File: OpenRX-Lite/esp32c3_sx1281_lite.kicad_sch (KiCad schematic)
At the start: 40 parts, among them U1 ESP32-C3FH4, U2 TLV75533PDQNR, U3 SX1281IMLTRT, U4 RFX2401C, X1 CJ17-400001010B20

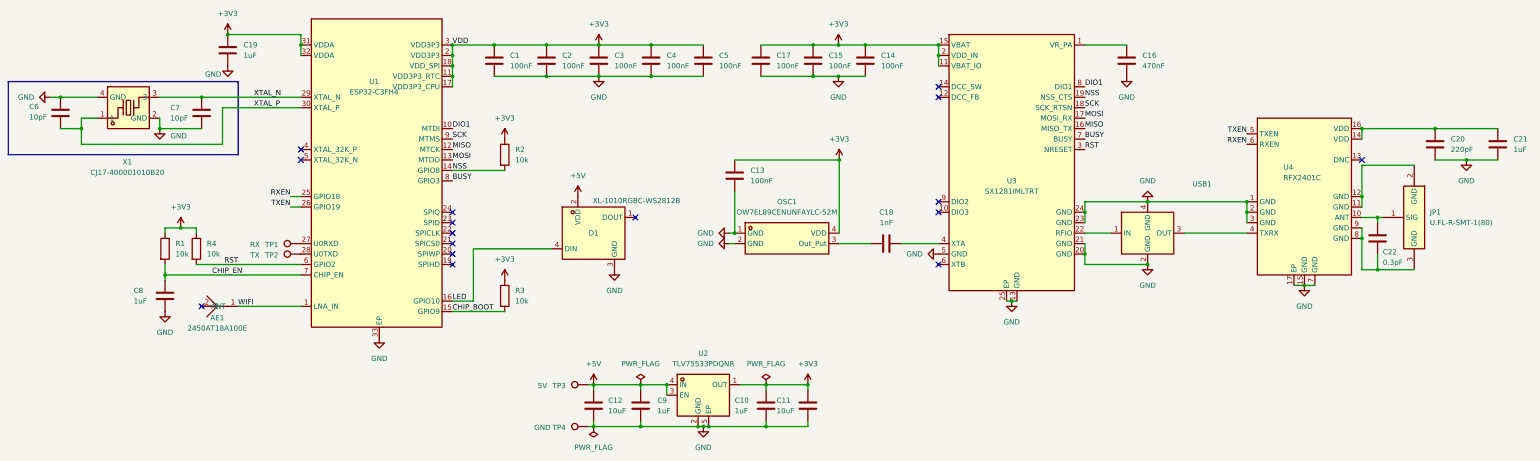
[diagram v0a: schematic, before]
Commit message: Separate Lite and Nano schematics, stop sharing one file
Sharing one .kicad_sch between projects doesn't work - KiCad
overwrites instance data when either project saves.

- Lite: restored pre-Nano schematic as local esp32c3_sx1281_lite.kicad_sch
- Nano: copied current shared sheet as local esp32c3_sx1281_rx_core.kicad_sch
- Each project now has its own schematic file
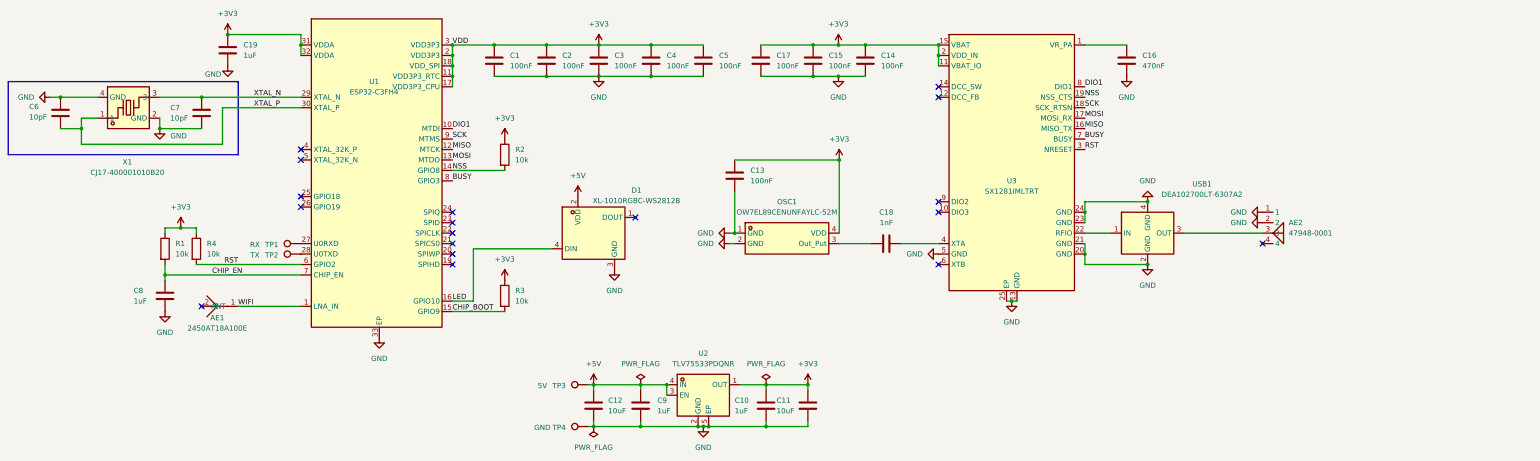
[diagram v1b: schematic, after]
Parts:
- removed C20: 220pF, Capacitor_SMD:C_0201_0603Metric, symbol Device:C
- removed C21: 1uF, Capacitor_SMD:C_0201_0603Metric, symbol Device:C
- removed C22: 0.3pF, Capacitor_SMD:C_0201_0603Metric, symbol Device:C
- removed JP1: U.FL-R-SMT-1(80), OpenRX-Shared:RF-SMD_FRF05002-JSS103M, symbol OpenRX-Shared:U.FL-R-SMT-1(80)
- removed U4: RFX2401C, OpenRX-Shared:QFN-16_L3.0-W3.0-P0.50-BL-EP1.7, symbol OpenRX-Shared:RFX2401C
- added AE2: 47948-0001, OpenRX-Shared:ANT-SMD_47948-0001, symbol OpenRX-Shared:47948-0001
- C1, C13, C14, C15, C17, C2, C3, C4, C5: LCSC C14858 -> (none)
- C10, C19, C8, C9: LCSC C77857 -> (none)
- C11, C12: LCSC C15525 -> (none)
- C16: LCSC C304534 -> (none)
- C18: LCSC C80390 -> (none)
- C6, C7: LCSC C14854 -> (none)
- R1, R2, R3, R4: LCSC C172043 -> (none)
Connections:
- net GND: now also AE2.1, AE2.2
- net at USB1.3 (OUT): now also AE2.3
- net RXEN: no longer names the net of U1.25 (GPIO18)
- net TXEN: no longer names the net of U1.26 (GPIO19)
- no-connect marks 16 -> 18

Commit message: Lite + Nano schematics: LCSC fields, fix 10uF to 0402, drop 0.3pF cap
- All passives in both schematics have LCSC fields
- 10uF caps fixed from 0201 to 0402 (C15525)
- Nano C22 (0.3pF): removed discrete cap, use trace capacitance instead
- 0 ERC errors on both schematics
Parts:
- AE1: LCSC (none) -> C89334
- AE2: LCSC (none) -> C152351
- C1, C13, C14, C15, C17, C2, C3, C4, C5: LCSC (none) -> C14858
- C10, C19, C8, C9: LCSC (none) -> C77857
- C11, C12: footprint Capacitor_SMD:C_0201_0603Metric -> Capacitor_SMD:C_0402_1005Metric; LCSC (none) -> C15525
- C16: LCSC (none) -> C304534
- C18: LCSC (none) -> C80390
- C6, C7: LCSC (none) -> C14854
- D1: LCSC (none) -> C5349953
- OSC1: LCSC (none) -> C22434896
- R1, R2, R3, R4: LCSC (none) -> C172043
- U1: LCSC (none) -> C2858491
- U2: LCSC (none) -> C2861882
- U3: LCSC (none) -> C2151551
- USB1: LCSC (none) -> C574024
- X1: LCSC (none) -> C2875272

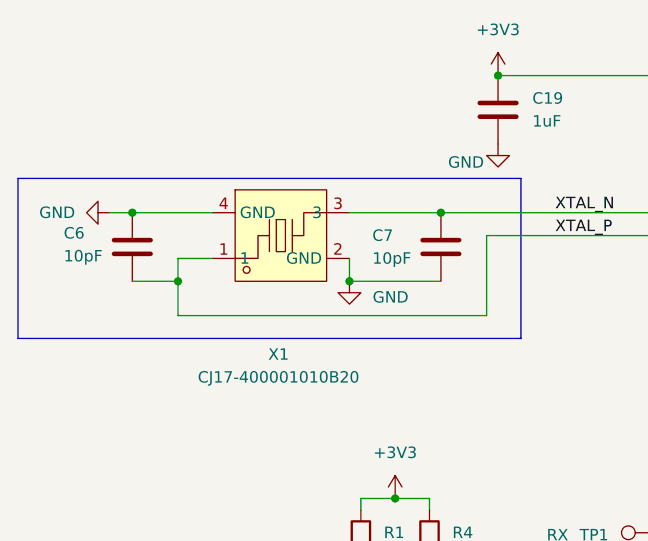
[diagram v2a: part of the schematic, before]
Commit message: Fix crystal load caps: 10pF → 18pF (C71153) on all 4 receivers
CJ17-400001010B20 crystal has CL=10pF. With 10pF load caps and
~2pF stray, effective load was only 7pF (30% low). Changed to 18pF
giving ~11pF effective load, matching the crystal spec.

C71153 = Samsung CL03C180JA3NNNC, 18pF C0G 25V 0201.
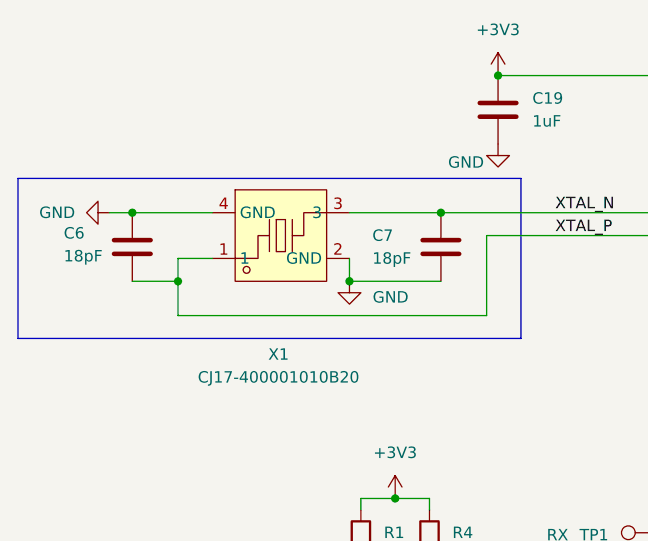
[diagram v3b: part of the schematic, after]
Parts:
- C6, C7: value 10pF -> 18pF; LCSC C14854 -> C71153
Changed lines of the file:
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@@
 			)
 		)
-		(property "Value" "10pF"
+		(property "Value" "18pF"
 			(at 66.04 46.99 0)
 			(show_name no)
@@
 			)
 		)
-		(property "LCSC" "C14854"
+		(property "LCSC" "C71153"
 			(at 0 0 0)
 			(show_name no)
@@
 			)
 		)
-		(property "Value" "10pF"
+		(property "Value" "18pF"
 			(at 31.75 46.736 0)
 			(show_name no)
@@
 			)
 		)
-		(property "LCSC" "C14854"
+		(property "LCSC" "C71153"
 			(at 0 0 0)
 			(show_name no)

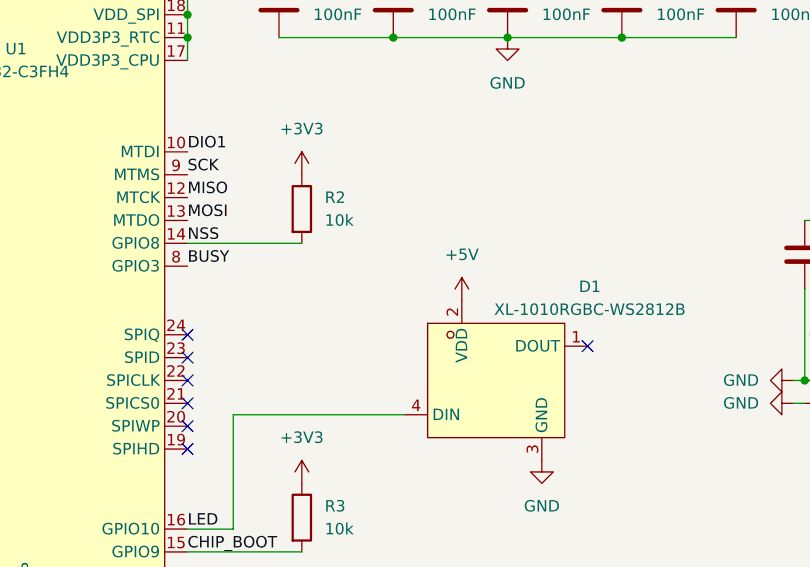
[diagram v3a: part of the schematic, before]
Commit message: Fix Gemini crystal load caps to 18pF (C62164), matching Lite and Mono
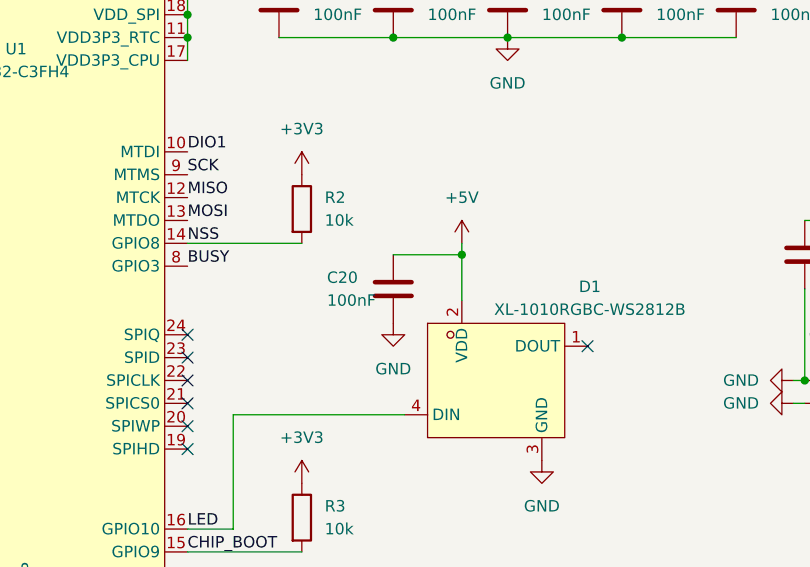
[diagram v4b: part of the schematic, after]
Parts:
- added C20: 100nF, Capacitor_SMD:C_0201_0603Metric, symbol Device:C
- C1, C13, C14, C15, C17, C2, C3, C4, C5: LCSC C14858 -> C76939
- C10, C19, C8, C9: LCSC C77857 -> C76935
- C16: LCSC C304534 -> C85926
- C18: LCSC C80390 -> C66942
- C6, C7: LCSC C71153 -> C62164
- R1, R2, R3, R4: LCSC C172043 -> C106225
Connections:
- net +5V: now also C20.1
- net GND: now also C20.2

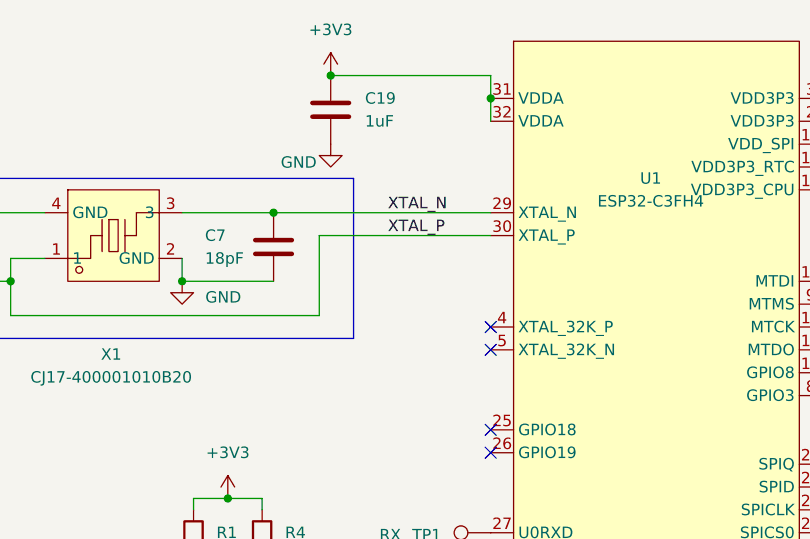
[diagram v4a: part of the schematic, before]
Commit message: OpenRX-Gemini: dual LR1121 schematic complete, 0 ERC errors
- Radio 1 (U4): sub-GHz via Johanson IPD → JP1 UFL
- Radio 2 (U9): 2.4GHz via RFX2401C (U10) → DEA (USB2) → JP3 UFL
- Shared SPI bus (SCK/MISO/MOSI), separate NSS/IRQ/BUSY/RST per radio
- Radio 2 control: GPIO10=NSS2, GPIO9=IRQ2, GPIO1=BUSY2, GPIO0=RST2
- FEM driven by Radio 2 RFSW (DIO5→RXEN, DIO6→TXEN)
- Radio 1 DIO5/DIO6 have 100k pull-downs (disconnected from FEM)
- No LED (GPIO10 used for NSS2), no boot button (GPIO9 used for IRQ2)
- Still needs: 10k pull-up on NSS2
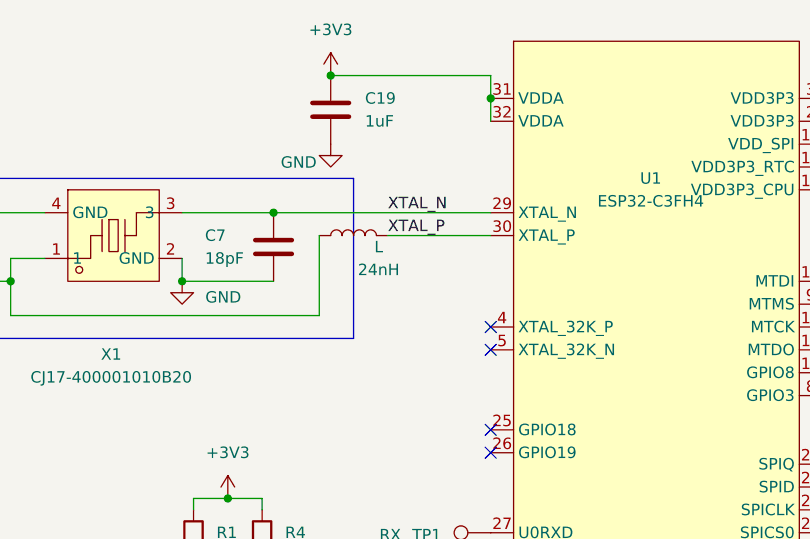
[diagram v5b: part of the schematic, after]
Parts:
- added L: 24nH, Inductor_SMD:L_0201_0603Metric, symbol Device:L
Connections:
- net XTAL_P: now also L.2; no longer C6.1, X1.1
- new net: C6.1, L.1, X1.1
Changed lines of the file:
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@@
+	(wire
+		(pts
+			(xy 86.36 44.45) (xy 97.79 44.45)
+		)
+		(stroke
+			(width 0)
+			(type default)
+		)
+	)
 	(wire
 		(pts
@@
 		(pts
 			(xy 64.77 85.09) (xy 64.77 82.55)
-		)
-		(stroke
-			(width 0)
-			(type default)
-		)
-	)
-	(wire
-		(pts
-			(xy 78.74 44.45) (xy 97.79 44.45)
 		)
 		(stroke
@@
 					(unit 1)
 				)
+			)
+		)
+	)
+	(symbol
+		(lib_id "Device:L")
+		(at 82.55 44.45 90)
+		(unit 1)
+		(body_style 1)
+		(exclude_from_sim no)
+		(in_bom yes)
+		(on_board yes)
+		(in_pos_files yes)
+		(dnp no)
+		(property "Reference" "L"
+			(at 85.344 45.72 90)
+			(show_name no)
+			(do_not_autoplace no)
+			(effects
+				(font
+					(size 1.27 1.27)
+				)
+			)
+		)
+		(property "Value" "24nH"
+			(at 85.344 48.26 90)
+			(show_name no)
+			(do_not_autoplace no)
+			(effects
+				(font
+					(size 1.27 1.27)
+				)
+			)
+		)
+		(property "Footprint" "Inductor_SMD:L_0201_0603Metric"
+			(at 82.55 44.45 0)
+			(hide yes)
+			(show_name no)
+			(do_not_autoplace no)
+			(effects
+				(font
+					(size 1.27 1.27)
+				)
+			)
+		)
+		(property "Datasheet" ""
+			(at 82.55 44.45 0)
+			(hide yes)
+			(show_name no)
+			(do_not_autoplace no)
+			(effects
+				(font
+					(size 1.27 1.27)
+				)
+			)
+		)
+		(property "Description" "Inductor"
+			(at 82.55 44.45 0)
+			(hide yes)
+			(show_name no)
+			(do_not_autoplace no)
+			(effects
+				(font
+					(size 1.27 1.27)
+				)
+			)
+		)
+		(property "LCSC" "C206441"
+			(at 82.55 44.45 0)
+			(hide yes)
+			(show_name no)
+			(do_not_autoplace no)
+			(effects
+				(font
+					(size 1.27 1.27)
+				)
+			)
+		)
+		(pin "2"
+		)
+		(pin "1"
+		)
+		(instances
+			(project "OpenRX-Lite"
+				(path "/8521861a-4fab-458b-8289-5e2efb91d906/d4225140-81df-42e7-abd7-e679e5ab5187"
+					(reference "L")
+					(unit 1)
+				)

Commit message: Swap all solder pads to 1.2x2.0mm rounded (25%) across Lite, Mono, Gemini
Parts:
- TP1, TP2, TP3, TP4: footprint OpenRX-Shared:SolderPad_1.0x1.5mm -> OpenRX-Shared:SolderPad_1.2x2.0mm
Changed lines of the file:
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@@
 			)
 		)
-		(property "Footprint" "OpenRX-Shared:SolderPad_1.0x1.5mm"
+		(property "Footprint" "OpenRX-Shared:SolderPad_1.2x2.0mm"
 			(at 167.64 116.84 0)
 			(hide yes)
@@
 			)
 		)
-		(property "Footprint" "OpenRX-Shared:SolderPad_1.0x1.5mm"
+		(property "Footprint" "OpenRX-Shared:SolderPad_1.2x2.0mm"
 			(at 97.79 72.39 0)
 			(hide yes)
@@
 			)
 		)
-		(property "Footprint" "OpenRX-Shared:SolderPad_1.0x1.5mm"
+		(property "Footprint" "OpenRX-Shared:SolderPad_1.2x2.0mm"
 			(at 97.79 74.93 0)
 			(hide yes)
@@
 			)
 		)
-		(property "Footprint" "OpenRX-Shared:SolderPad_1.0x1.5mm"
+		(property "Footprint" "OpenRX-Shared:SolderPad_1.2x2.0mm"
 			(at 167.64 106.68 0)
 			(hide yes)

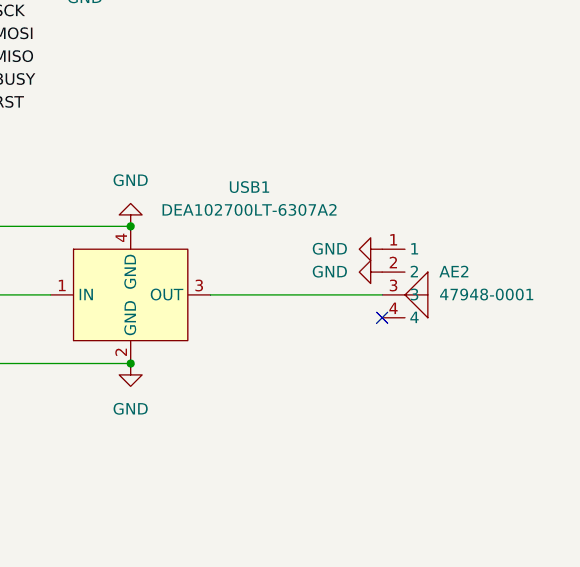
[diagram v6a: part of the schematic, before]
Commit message: Repo cleanup: final state for handoff
- Clean README with architecture, BOM, CE notes, status
- Remove dated analysis files (absorbed into FINAL_NETLIST + KICAD_WORKFLOW)
- Remove stale OpenRX-Dual (archived), ERC reports, backups, prl files
- Updated .gitignore for .kicad_dru, production backups
- CERN-OHL-S v2 license confirmed
- 3 active projects: Lite, Mono, Gemini
- Schematics final, initial PCB layouts done, routing in progress
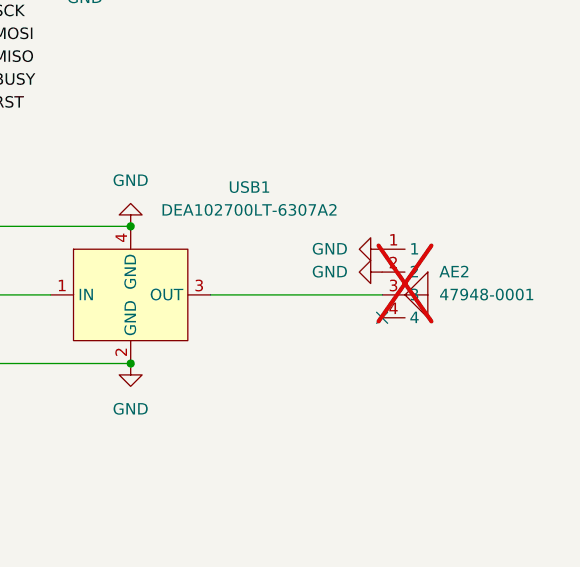
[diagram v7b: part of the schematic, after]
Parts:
- AE2: now not fitted
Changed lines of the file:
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@@
 		(on_board yes)
 		(in_pos_files yes)
-		(dnp no)
+		(dnp yes)
 		(fields_autoplaced yes)
 		(property "Reference" "AE2"
